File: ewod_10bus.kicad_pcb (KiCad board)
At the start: 2 copper layers, 100 x 100 mm, 45 parts, among them J1 B2P-VH, J2 B2P-VH, J3 B2P-VH, J4 B2P-VH, J5 B2P-VH, J6 B2P-VH, J7 B2P-VH, J8 Barrel_Jack, J9 031-5637, K1 AQV254A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

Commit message: Update!
- Added via shielding for signal integrity & EMC-related purposes.
- Removed excessive decoupling capacitors.
- Rerouted traces and slight repositioning to allow for shorter connections.
- Added GND pour for both sides for better manufacturability and EMC-related performance.
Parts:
- removed C1, C4, C7: 10 uF, Capacitor_SMD:C_0805_2012Metric
- removed C2: EEU-FR1A221, Capacitor_THT:CP_Radial_D6.3mm_P2.50mm
- removed C6: 100n, Capacitor_SMD:C_0603_1608Metric
- moved R3 46.9 mm to (154.7, 74.2), turned to 90 degrees
- moved R2 40.5 mm to (170.5, 74.2), turned to 90 degrees
- moved R1 39.7 mm to (186.4, 74.4), turned to 90 degrees
- moved J8 24.0 mm to (192.6, 109.7)
- moved C3 8.24 mm to (189.8, 110.3), turned to -90 degrees
- moved U1 5.84 mm to (172.0, 101.9)
- moved R4 5.84 mm to (167.8, 119.7)
- moved R5 5.84 mm to (167.8, 122.3)
- moved R6 5.84 mm to (167.8, 124.8)
- moved R7 5.84 mm to (167.8, 127.4)
- moved R14 2.48 mm to (130.1, 106.5)
- moved R13 2.43 mm to (130.1, 90.9)
- moved R12 2.40 mm to (130.0, 75.1)
- moved R11 0.08 mm to (150.1, 60.1)
- moved R8 0.07 mm to (196.9, 60.0)
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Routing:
- net /+5V: track 75.2 -> 6.11 mm
- net Net-(K3-A): track 64.7 -> 4.65 mm
- net Net-(K1-A): track 63.6 -> 4.87 mm
- net Net-(K2-A): track 57.0 -> 4.69 mm
- net Net-(U1-D4): track 3.41 -> 49.1 mm
- net Net-(U1-D2): track 3.42 -> 42.8 mm
- net Net-(U1-D3): track 3.42 -> 41.2 mm
- net AMP_GND: track 26.3 -> 0.00 mm, vias 8 -> 403
- net GND: track 19.6 -> 0.04 mm, vias 12 -> 405
- net Net-(K4-A): track 78.5 -> 62.3 mm
- net Net-(K5-A): track 67.8 -> 52.4 mm
- net Net-(K6-A): track 55.2 -> 40.5 mm
- net Net-(K7-A): track 43.7 -> 33.5 mm
- net /BUS4_HV: track 12.6 -> 9.62 mm
- net /BUS6_HV: track 11.5 -> 8.92 mm
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- added copper zone on F.Cu, net AMP_GND
- added copper zone on F.Cu, net GND

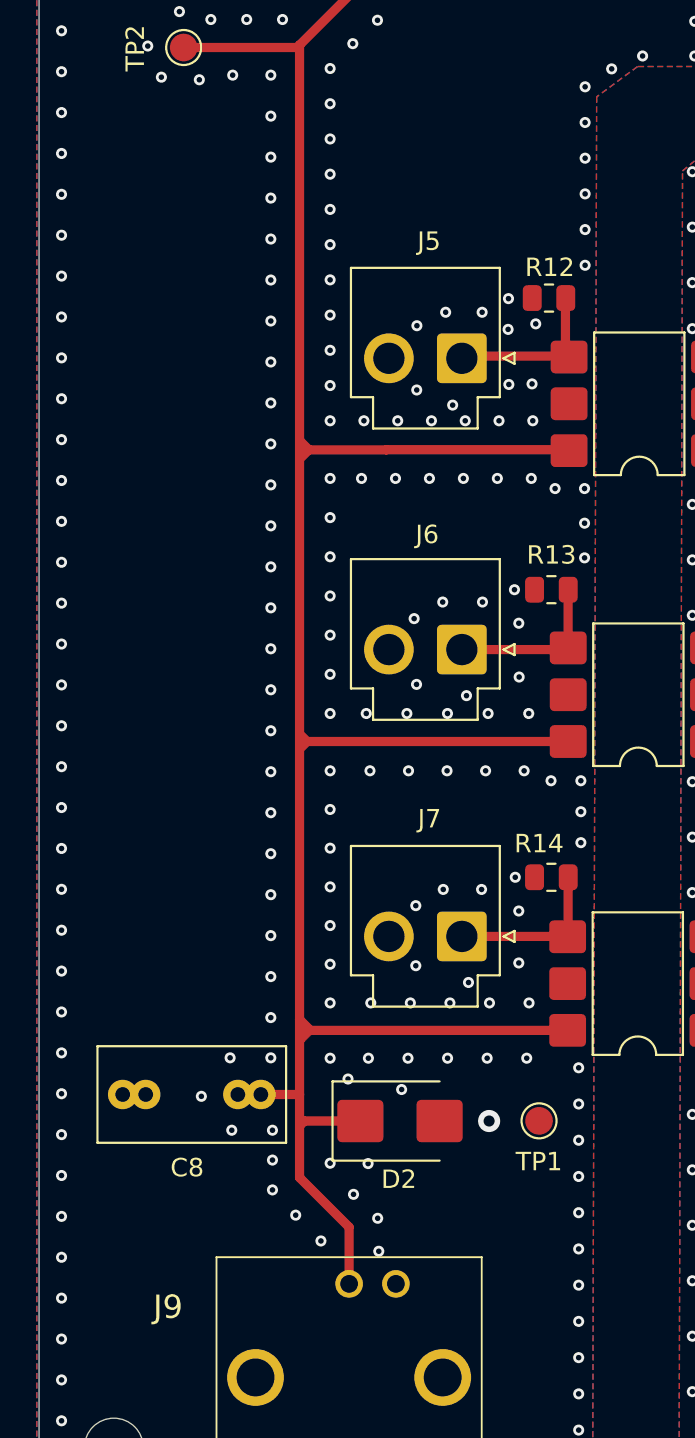
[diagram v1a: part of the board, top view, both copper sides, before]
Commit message: Update
Adjusted spacing of output capacitor HV side.
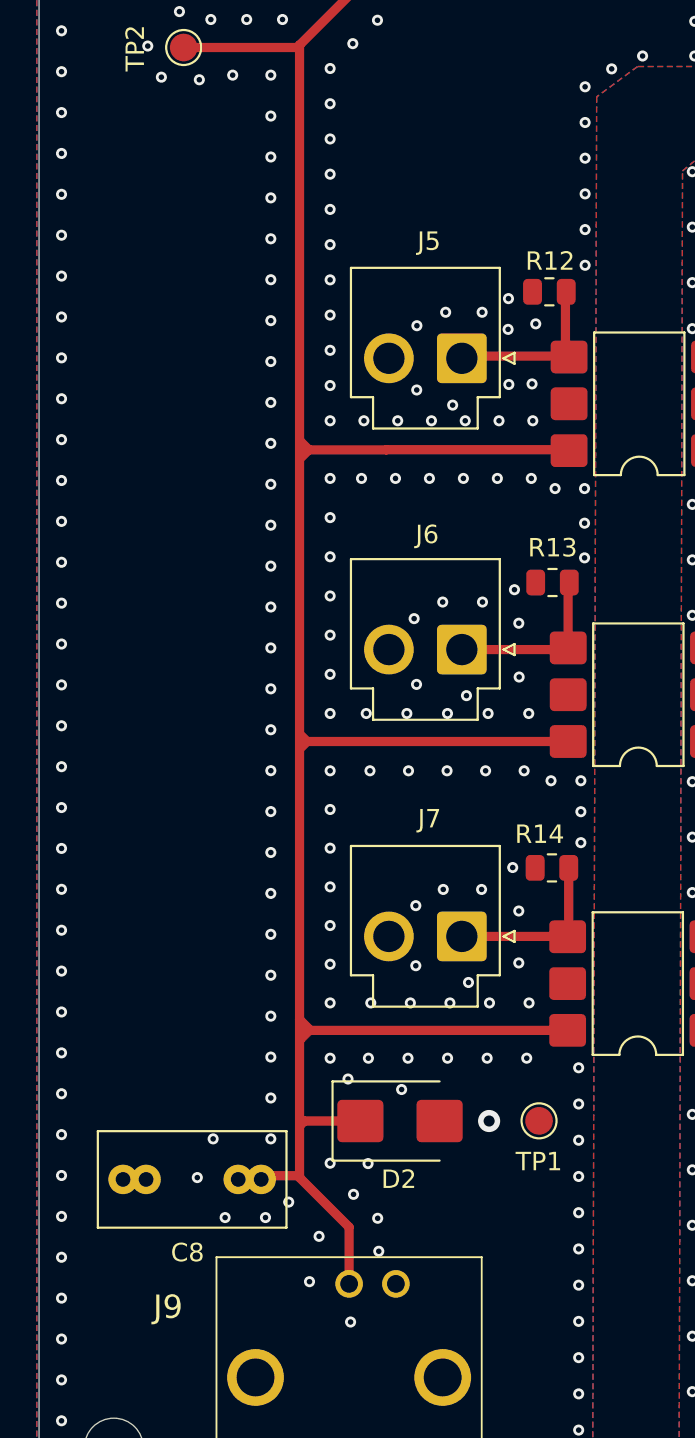
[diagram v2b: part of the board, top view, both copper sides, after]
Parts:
- moved C8 4.61 mm to (106.9, 123.0)
- moved R14 0.51 mm to (130.2, 106.0)
- moved R13 0.39 mm to (130.2, 90.5)
- moved R12 0.34 mm to (130.0, 74.8)
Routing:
- net /BUS6_HV: track 8.92 -> 9.96 mm
- net AMP_GND: vias 403 -> 405
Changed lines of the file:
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@@
 	(footprint "Resistor_SMD:R_0805_2012Metric"
 		(layer "F.Cu")
-		(at 130 75.11 180)
+		(at 130.02 74.77 180)
 		(descr "Resistor SMD 0805 (2012 Metric), square (rectangular) end terminal, IPC-7351 nominal, (Body size source: IPC-SM-782 page 72, https://www.pcb-3d.com/wordpress/wp-content/uploads/ipc-sm-782a_amendment_1_and_2.pdf), generated with kicad-footprint-generator")
 		(tags "resistor")
@@
 	(footprint "Capacitor_THT:C_Rect_L10.0mm_W5.0mm_P5.00mm_P7.50mm"
 		(layer "F.Cu")
-		(at 106.86 118.34)
+		(at 106.88 122.95)
 		(descr "C, Rect series, Radial, pin pitch=5.00mm 7.50mm, length*width=10*5mm^2, Capacitor")
 		(tags "C Rect series Radial pin pitch 5.00mm 7.50mm length 10mm width 5mm Capacitor")
@@
 	(footprint "Resistor_SMD:R_0805_2012Metric"
 		(layer "F.Cu")
-		(at 130.13 106.55 180)
+		(at 130.16 106.04 180)
 		(descr "Resistor SMD 0805 (2012 Metric), square (rectangular) end terminal, IPC-7351 nominal, (Body size source: IPC-SM-782 page 72, https://www.pcb-3d.com/wordpress/wp-content/uploads/ipc-sm-782a_amendment_1_and_2.pdf), generated with kicad-footprint-generator")
 		(tags "resistor")
@@
 	(footprint "Resistor_SMD:R_0805_2012Metric"
 		(layer "F.Cu")
-		(at 130.13 90.94 180)
+		(at 130.19 90.55 180)
 		(descr "Resistor SMD 0805 (2012 Metric), square (rectangular) end terminal, IPC-7351 nominal, (Body size source: IPC-SM-782 page 72, https://www.pcb-3d.com/wordpress/wp-content/uploads/ipc-sm-782a_amendment_1_and_2.pdf), generated with kicad-footprint-generator")
 		(tags "resistor")
@@
 	)
 	(via
-		(at 114.9 80.803333)
+		(at 114.9 80.776154)
 		(size 0.6)
 		(drill 0.3)
@@
 	)
 	(via
-		(at 114.99 121.9)
-		(size 0.6)
-		(drill 0.3)
-		(layers "F.Cu" "B.Cu")
-		(free yes)
-		(net 3)
-	)
-	(via
-		(at 114.9 91.924167)
+		(at 114.9 91.88)
 		(size 0.6)
 		(drill 0.3)
@@
 	)
 	(via
-		(at 114.9 89.7)
+		(at 114.9 89.659231)
 		(size 0.6)
 		(drill 0.3)
@@
 	)
 	(via
-		(at 114.9 114.165833)
+		(at 114.9 114.087692)
 		(size 0.6)
 		(drill 0.3)
@@
 	)
 	(via
-		(at 114.9 78.579167)
+		(at 114.9 78.555385)
 		(size 0.6)
 		(drill 0.3)
@@
 	)
 	(via
+		(at 117 128.5)
+		(size 0.6)
+		(drill 0.3)
+		(layers "F.Cu" "B.Cu")
+		(free yes)
+		(net 3)
+	)
+	(via
 		(at 157.712222 43.15)
 		(size 0.6)
@@
 	)
 	(via
-		(at 112.78 120.28)
+		(at 114.9 120.75)
 		(size 0.6)
 		(drill 0.3)
@@
 	)
 	(via
-		(at 114.9 76.355)
+		(at 114.9 76.334615)
 		(size 0.6)
 		(drill 0.3)
@@
 	)
 	(via
-		(at 114.99 123.52)
-		(size 0.6)
-		(drill 0.3)
-		(layers "F.Cu" "B.Cu")
-		(free yes)
-		(net 3)
-	)
-	(via
 		(at 141.460556 43.15)
 		(size 0.6)
@@
 	)
 	(via
-		(at 114.9 96.3725)
+		(at 114.9 96.321538)
 		(size 0.6)
 		(drill 0.3)
@@
 	)
 	(via
-		(at 114.9 71.906667)
+		(at 114.9 71.893077)
 		(size 0.6)
 		(drill 0.3)
@@
 	)
 	(via
-		(at 114.9 107.493333)
+		(at 114.9 107.425385)
 		(size 0.6)
 		(drill 0.3)
@@
 	)
 	(via
-		(at 114.9 116.35)
+		(at 114.9 116.308462)
+		(size 0.6)
+		(drill 0.3)
+		(layers "F.Cu" "B.Cu")
+		(free yes)
+		(net 3)
+	)
+	(via
+		(at 112.42 125.02)
 		(size 0.6)
 		(drill 0.3)
@@
 	)
 	(via
-		(at 114.9 85.251667)
+		(at 114.9 85.217692)
 		(size 0.6)
 		(drill 0.3)
@@
 	)
 	(via
-		(at 114.9 65.234167)
+		(at 114.9 65.230769)
 		(size 0.6)
 		(drill 0.3)
@@
 	)
 	(via
-		(at 114.9 105.269167)
+		(at 114.9 105.204615)
 		(size 0.6)
 		(drill 0.3)
@@
 	)
 	(via
-		(at 117.62 126.29)
-		(size 0.6)
-		(drill 0.3)
-		(layers "F.Cu" "B.Cu")
-		(free yes)
-		(net 3)
-	)
-	(via
 		(at 118.12 116.37)
 		(size 0.6)
@@
 	)
 	(via
-		(at 114.9 103.045)
+		(at 114.9 102.983846)
 		(size 0.6)
 		(drill 0.3)
@@
 	)
 	(via
-		(at 114.9 87.475833)
+		(at 114.9 87.438462)
 		(size 0.6)
 		(drill 0.3)
@@
 	)
 	(via
-		(at 128.17 106.55)
+		(at 128.03 106.02)
 		(size 0.6)
 		(drill 0.3)
@@
 	)
 	(via
-		(at 114.9 74.130833)
+		(at 114.9 74.113846)
 		(size 0.6)
 		(drill 0.3)
@@
 	)
 	(via
+		(at 114.61 125.02)
+		(size 0.6)
+		(drill 0.3)
+		(layers "F.Cu" "B.Cu")
+		(free yes)
+		(net 3)
+	)
+	(via
 		(at 193.94 56.09)
 		(size 0.6)
@@
 	)
 	(via
-		(at 114.99 120.28)
+		(at 114.9 118.529231)
 		(size 0.6)
 		(drill 0.3)
@@
 	)
 	(via
+		(at 119.23 130.69)
+		(size 0.6)
+		(drill 0.3)
+		(layers "F.Cu" "B.Cu")
+		(free yes)
+		(net 3)
+	)
+	(via
 		(at 126.34 107.21)
 		(size 0.6)
@@
 	)
 	(via
-		(at 114.9 94.148333)
+		(at 114.9 94.100769)
 		(size 0.6)
 		(drill 0.3)
@@
 	)
 	(via
-		(at 114.9 69.6825)
+		(at 114.9 69.672308)
 		(size 0.6)
 		(drill 0.3)
@@
 	)
 	(via
-		(at 114.9 109.7175)
+		(at 114.9 109.646154)
 		(size 0.6)
 		(drill 0.3)
@@
 	)
 	(via
-		(at 114.9 111.941667)
+		(at 114.9 111.866923)
 		(size 0.6)
 		(drill 0.3)
@@
 	)
 	(via
-		(at 114.9 100.820833)
+		(at 114.9 100.763077)
 		(size 0.6)
 		(drill 0.3)
@@
 	)
 	(via
-		(at 111.13 118.44)
+		(at 111.77 120.75)
 		(size 0.6)
 		(drill 0.3)
@@
 	)
 	(via
+		(at 115.87 124.18)
+		(size 0.6)
+		(drill 0.3)
+		(layers "F.Cu" "B.Cu")
+		(free yes)
+		(net 3)
+	)
+	(via
 		(at 179.381111 43.15)
 		(size 0.6)
@@
 	)
 	(via
-		(at 114.9 98.596667)
+		(at 114.9 98.542308)
 		(size 0.6)
 		(drill 0.3)
@@
 	)
 	(via
-		(at 116.25 124.89)
-		(size 0.6)
-		(drill 0.3)
-		(layers "F.Cu" "B.Cu")
-		(free yes)
-		(net 3)
-	)
-	(via
 		(at 172.11 53.135)
 		(size 0.6)
@@
 	)
 	(via
-		(at 112.69 116.35)
+		(at 110.91 122.85)
 		(size 0.6)
 		(drill 0.3)
@@
 	)
 	(via
-		(at 114.9 83.0275)
+		(at 114.9 82.996923)
 		(size 0.6)
 		(drill 0.3)
@@
 	)
 	(via
-		(at 114.9 67.458333)
+		(at 114.9 67.451538)
 		(size 0.6)
 		(drill 0.3)
@@
 	)
 	(via
+		(at 117.52 126.04)
+		(size 0.6)
+		(drill 0.3)
+		(layers "F.Cu" "B.Cu")
+		(free yes)
+		(net 3)
+	)
+	(via
 		(at 125.07 50.22)
 		(size 0.6)
@@
 	)
 	(segment
-		(start 116.96 83.35)
-		(end 116.46 83.35)
+		(start 114.581 122.749)
+		(end 116.46 122.749)
 		(width 0.5)
 		(layer "F.Cu")
@@
 	)
 	(segment
-		(start 116.46 120.05)
-		(end 116.46 118.34)
+		(start 116.96 83.35)
+		(end 116.46 83.35)
 		(width 0.5)
 		(layer "F.Cu")
@@
 	)
 	(segment
-		(start 114.36 118.34)
-		(end 116.46 118.34)
-		(width 0.5)
-		(layer "F.Cu")
-		(net 4)
-	)
-	(segment
 		(start 121.16 83.35)
 		(end 116.96 83.35)
@@
 	)
 	(segment
-		(start 116.46 118.34)
+		(start 116.46 120.05)
 		(end 116.46 115.4)
 		(width 0.5)
@@
 	)
 	(segment
-		(start 130.8925 75.13)
+		(start 130.9325 74.77)
+		(end 130.8925 74.81)
+		(width 0.5)
+		(layer "F.Cu")
+		(net 9)
+	)
+	(segment
+		(start 130.8925 74.81)
 		(end 130.8925 78.0875)
 		(width 0.5)
@@
 	)
 	(segment
+		(start 131.04 94.1)
+		(end 131.04 90.6425)
+		(width 0.5)
+		(layer "F.Cu")
+		(net 10)
+	)
+	(segment
 		(start 125.27 94.19)
 		(end 130.95 94.19)
@@
 	)
 	(segment
-		(start 131.04 94.1)
-		(end 131.04 90.9125)
+		(start 131.04 90.6425)
+		(end 131.1025 90.58)
 		(width 0.5)
 		(layer "F.Cu")
@@
 	)
 	(segment
+		(start 131.0725 109.7175)
+		(end 131.0425 109.7475)
+		(width 0.5)
+		(layer "F.Cu")
+		(net 11)
+	)
+	(segment
+		(start 131.0725 106.52)
+		(end 131.0725 106.04)
+		(width 0.5)
+		(layer "F.Cu")
+		(net 11)
+	)
+	(segment
 		(start 125.27 109.76)
 		(end 130.99 109.76)
@@
 	)
 	(segment
+		(start 131.0725 106.04)
+		(end 131.0725 109.7175)
+		(width 0.5)
+		(layer "F.Cu")
+		(net 11)
+	)
+	(segment
 		(start 131.0425 106.55)
-		(end 131.0425 109.7475)
+		(end 131.0725 106.52)
 		(width 0.5)
 		(layer "F.Cu")
